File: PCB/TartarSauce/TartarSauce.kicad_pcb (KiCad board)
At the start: 2 copper layers, 118.1 x 76.2 mm, 46 parts, among them J1 Thumbstick, J2 OLED, J3 Conn_01x02, J4 Conn_01x02, U1 Teensy4.0, U2 MIC4801

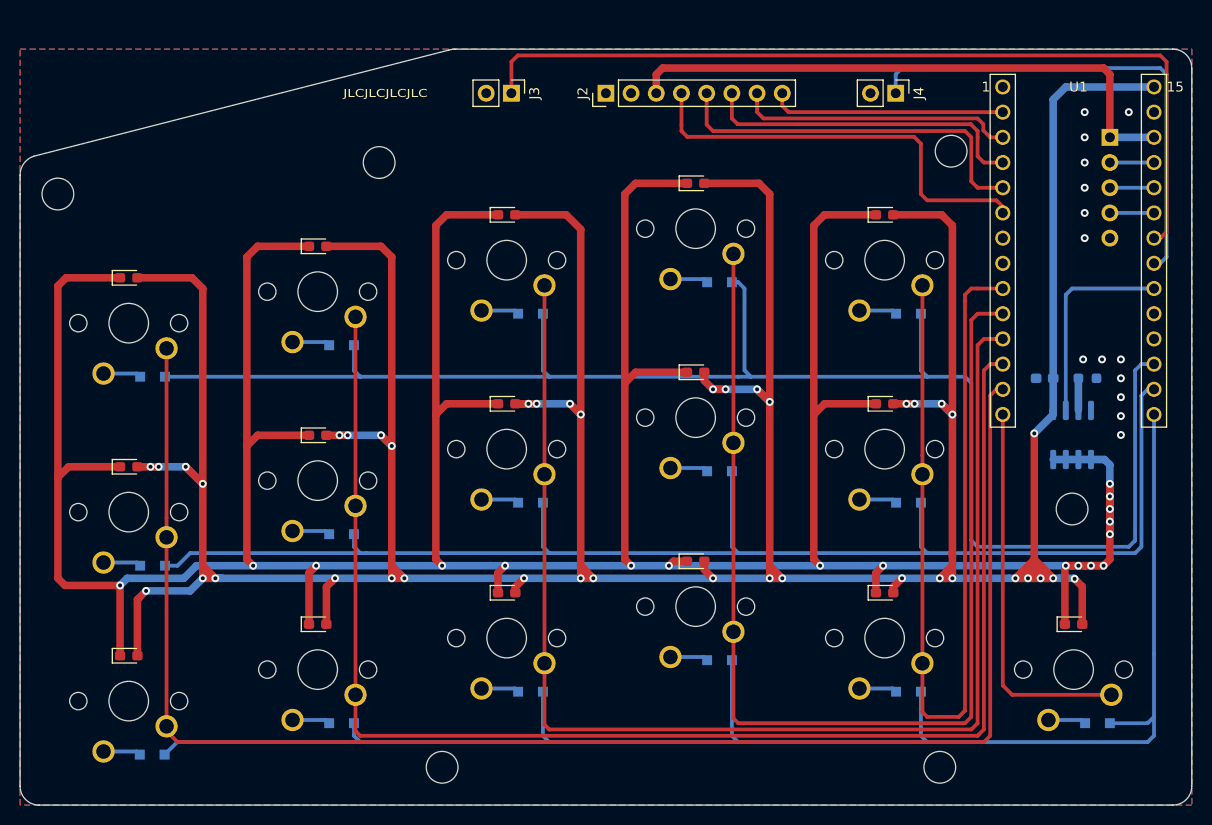
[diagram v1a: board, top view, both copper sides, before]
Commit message: Changed project to PlatformIO, added bitmaps and saved STL files to repo
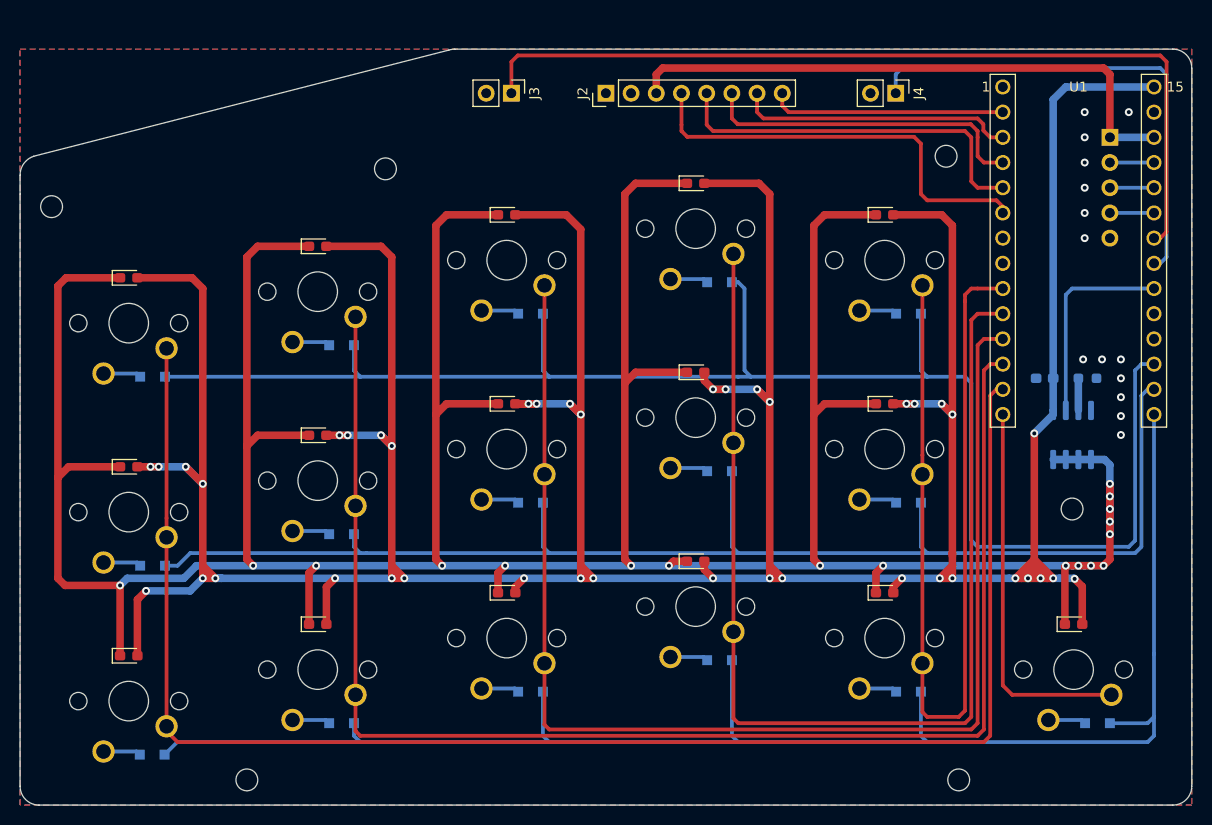
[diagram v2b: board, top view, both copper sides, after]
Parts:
- removed the REF** at (123.1, 42.7)
- removed the REF** at (135.3, 78.7)
- removed the REF** at (65.4, 43.8)
- removed the REF** at (33.0, 47.0)
- removed the REF** at (71.8, 104.8)
- removed the REF** at (121.9, 104.8)
- added REF**: MountingHole_2.2mm_M2, MountingHole:MountingHole_2.2mm_M2, F.Cu at (135.3, 78.7)
- added REF**: MountingHole_2.2mm_M2, MountingHole:MountingHole_2.2mm_M2, F.Cu at (123.8, 106.0)
- added REF**: MountingHole_2.2mm_M2, MountingHole:MountingHole_2.2mm_M2, F.Cu at (52.1, 106.0)
- added REF**: MountingHole_2.2mm_M2, MountingHole:MountingHole_2.2mm_M2, F.Cu at (66.0, 44.5)
- added REF**: MountingHole_2.2mm_M2, MountingHole:MountingHole_2.2mm_M2, F.Cu at (122.6, 43.2)
- added REF**: MountingHole_2.2mm_M2, MountingHole:MountingHole_2.2mm_M2, F.Cu at (32.4, 48.3)

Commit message: Joystick works now, but isn't scaled properly
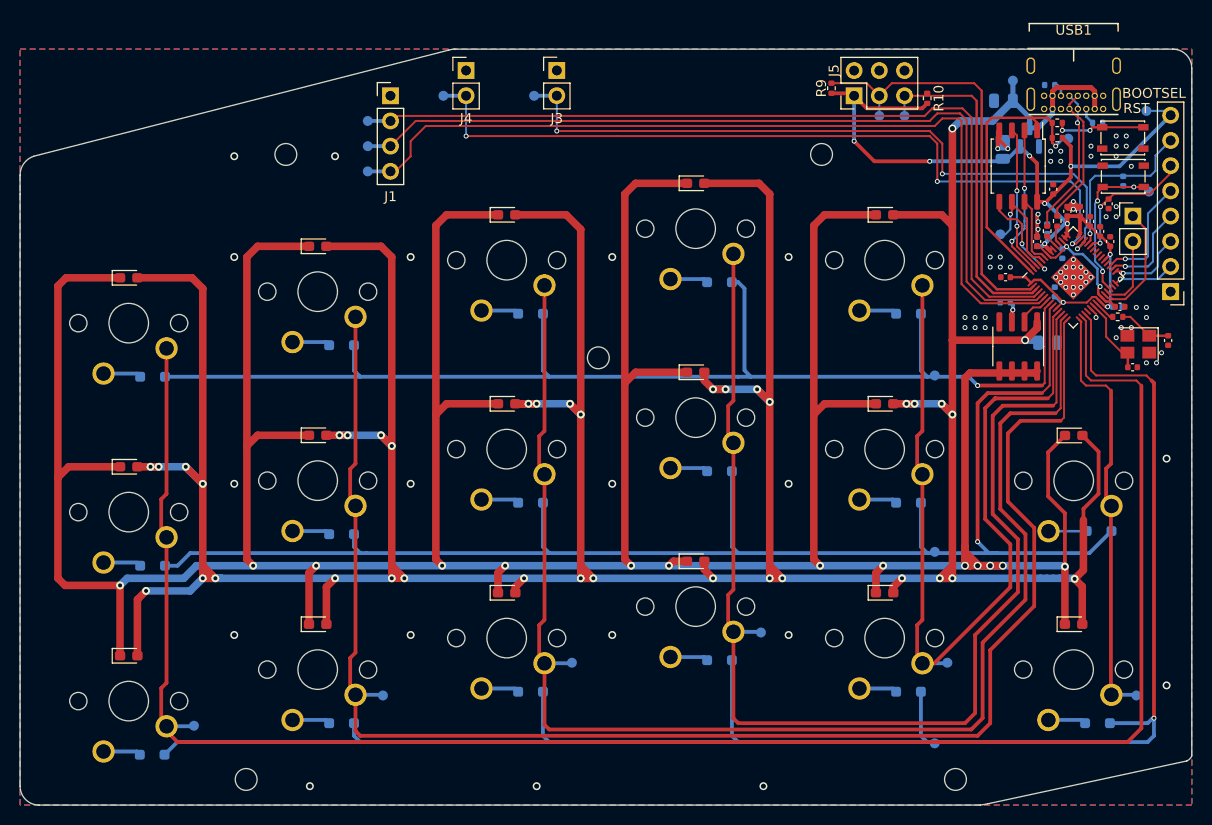
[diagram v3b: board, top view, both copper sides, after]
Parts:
- removed the REF** at (135.3, 78.7)
- removed the REF** at (123.8, 106.0)
- removed the REF** at (52.1, 106.0)
- removed the REF** at (66.0, 44.5)
- removed the REF** at (122.6, 43.2)
- removed the REF** at (32.4, 48.3)
- removed U1: Teensy4.0, _MCU_Devboards:Teensy4.0
- added C10: 0.1u, Capacitor_SMD:C_0402_1005Metric, F.Cu at (138.1, 50.8)
- added C11: 0.1u, Capacitor_SMD:C_0402_1005Metric, F.Cu at (137.1, 49.7)
- added C12: 0.1u, Capacitor_SMD:C_0402_1005Metric, F.Cu at (128.6, 55.4)
- added C13: 0.1u, Capacitor_SMD:C_0402_1005Metric, B.Cu at (133.5, 56.9)
- added C14: 0.1u, Capacitor_SMD:C_0402_1005Metric, B.Cu at (139.8, 58.4)
- added C15: 0.1u, Capacitor_SMD:C_0402_1005Metric, F.Cu at (133.3, 46.5)
- added C16: 27p, Capacitor_SMD:C_0402_1005Metric, F.Cu at (141.4, 64.5)
- added C17: 27p, Capacitor_SMD:C_0402_1005Metric, F.Cu at (144.9, 61.8)
- added C18: 10u, Capacitor_SMD:C_0805_2012Metric, B.Cu at (128.3, 37.6)
- added C19: 10u, Capacitor_SMD:C_0805_2012Metric, B.Cu at (128.3, 42.5)
- added C2: 1u, Capacitor_SMD:C_0402_1005Metric, B.Cu at (134.3, 53.0)
- added C20: 1n, Capacitor_SMD:C_0402_1005Metric, B.Cu at (140.4, 45.7)
- added C21: 1n, Capacitor_SMD:C_0402_1005Metric, F.Cu at (138.9, 48.0)
- added C3: 0.1u, Capacitor_SMD:C_0402_1005Metric, F.Cu at (131.7, 51.8)
- added C4: 0.1u, Capacitor_SMD:C_0402_1005Metric, F.Cu at (140.1, 58.4)
- added C5: 1u, Capacitor_SMD:C_0402_1005Metric, F.Cu at (136.0, 48.7)
- added C6: 0.1u, Capacitor_SMD:C_0402_1005Metric, B.Cu at (132.7, 50.5)
- added C7: 0.1u, Capacitor_SMD:C_0402_1005Metric, F.Cu at (134.8, 48.7)
- added C8: 0.1u, Capacitor_SMD:C_0402_1005Metric, F.Cu at (139.1, 51.8)
- added C9: 0.1u, Capacitor_SMD:C_0402_1005Metric, B.Cu at (131.7, 51.8)
- added D17: D, Diode_SMD:D_SOD-323_HandSoldering, B.Cu at (138.0, 81.0)
- added J5: OLED, Connector_PinHeader_2.54mm:PinHeader_2x03_P2.54mm_Vertical, F.Cu at (113.3, 37.1)
- added J6: DBG, Connector_PinHeader_2.54mm:PinHeader_1x02_P2.54mm_Vertical, F.Cu at (141.4, 49.2)
- added MX17: MX-LED, MX_Only:MXOnly-1U, F.Cu at (125.9, 66.4)
- added R10: 5k1, Resistor_SMD:R_0402_1005Metric, F.Cu at (120.7, 37.3)
- added R2: DNP, Resistor_SMD:R_0402_1005Metric, F.Cu at (133.8, 41.3)
- added R3: 1k, Resistor_SMD:R_0402_1005Metric, F.Cu at (133.8, 39.8)
- added R4: 1k, Resistor_SMD:R_0402_1005Metric, F.Cu at (139.9, 59.4)
- added R5: 5k1, Resistor_SMD:R_0402_1005Metric, B.Cu at (137.8, 39.8)
- added R6: 5k1, Resistor_SMD:R_0402_1005Metric, B.Cu at (133.0, 36.0)
- added R7: 27R, Resistor_SMD:R_0402_1005Metric, F.Cu at (133.8, 49.7)
- added R8: 27R, Resistor_SMD:R_0402_1005Metric, F.Cu at (132.7, 50.7)
- added R9: 5k1, Resistor_SMD:R_0402_1005Metric, F.Cu at (111.0, 36.3)
- added REF**: MountingHole_2.2mm_M2, MountingHole:MountingHole_2.2mm_M2, F.Cu at (110.0, 43.0)
- added REF**: MountingHole_2.2mm_M2, MountingHole:MountingHole_2.2mm_M2, F.Cu at (87.5, 63.5)
- added REF**: MountingHole_2.2mm_M2, MountingHole:MountingHole_2.2mm_M2, F.Cu at (52.0, 106.0)
- added REF**: MountingHole_2.2mm_M2, MountingHole:MountingHole_2.2mm_M2, F.Cu at (56.0, 43.0)
- added REF**: MountingHole_2.2mm_M2, MountingHole:MountingHole_2.2mm_M2, F.Cu at (123.5, 106.0)
- added SW1: BOOTSEL, Button_Switch_SMD:SW_SPST_PTS810, F.Cu at (140.4, 41.3)
- added SW2: RST, Button_Switch_SMD:SW_SPST_PTS810, F.Cu at (140.4, 45.2)
- added TP1: ROW0, TestPoint:TestPoint_Pad_D1.0mm, B.Cu at (121.4, 65.3)
- added TP10: SDA, TestPoint:TestPoint_Pad_D1.0mm, B.Cu at (115.8, 39.1)
- added TP11: SCL, TestPoint:TestPoint_Pad_D1.0mm, B.Cu at (118.4, 39.1)
- added TP13: ENCA, TestPoint:TestPoint_Pad_D1.0mm, B.Cu at (64.3, 39.6)
- added TP14: ENCB, TestPoint:TestPoint_Pad_D1.0mm, B.Cu at (64.3, 42.2)
- added TP15: ENCC, TestPoint:TestPoint_Pad_D1.0mm, B.Cu at (64.3, 44.7)
- added TP16: MISCA, TestPoint:TestPoint_Pad_D1.0mm, B.Cu at (81.0, 37.1)
- added TP17: MISCB, TestPoint:TestPoint_Pad_D1.0mm, B.Cu at (71.9, 37.1)
- added TP2: ROW1, TestPoint:TestPoint_Pad_D1.0mm, B.Cu at (121.4, 83.1)
- added TP28: SCK, TestPoint:TestPoint_Pad_D1.0mm, B.Cu at (128.0, 51.1)
- added TP29: SCK, TestPoint:TestPoint_Pad_D1.0mm, B.Cu at (134.9, 41.4)
- added TP3: ROW2, TestPoint:TestPoint_Pad_D1.0mm, B.Cu at (121.4, 102.4)
- added TP31: RUN, TestPoint:TestPoint_Pad_D1.0mm, B.Cu at (143.0, 46.7)
- added TP32: 5V, TestPoint:TestPoint_Pad_D1.0mm, B.Cu at (129.3, 35.6)
- added TP33: 3V3, TestPoint:TestPoint_Pad_D1.0mm, B.Cu at (142.7, 38.6)
- added TP4: COL0, TestPoint:TestPoint_Pad_D1.0mm, B.Cu at (46.7, 100.6)
- added TP5: COL1, TestPoint:TestPoint_Pad_D1.0mm, B.Cu at (65.8, 97.5)
- added TP6: COL2, TestPoint:TestPoint_Pad_D1.0mm, B.Cu at (84.8, 94.2)
- added TP7: COL3, TestPoint:TestPoint_Pad_D1.0mm, B.Cu at (103.9, 91.2)
- added TP8: COL4, TestPoint:TestPoint_Pad_D1.0mm, B.Cu at (122.7, 94.2)
- added TP9: COL5, TestPoint:TestPoint_Pad_D1.0mm, B.Cu at (141.7, 97.5)
- added U3: RP2040, Package_DFN_QFN:QFN-56-1EP_7x7mm_P0.4mm_EP3.2x3.2mm, F.Cu at (135.4, 55.4)
- added U4: W25Q128JVS, Package_SO:SOIC-8_5.23x5.23mm_P1.27mm, F.Cu at (129.8, 44.2)
- added U5: AP2127N-3.3, Package_TO_SOT_SMD:SOT-23, B.Cu at (131.0, 41.3)
- added USB1: USB4085-GF-A-Type-C, patchez_connectors:USB_C_GCT_USB4085, F.Cu at (135.4, 32.3)
- added Y1: 12MHz_18pf_30ppm, Crystal:Crystal_SMD_3225-4Pin_3.2x2.5mm, F.Cu at (141.9, 62.1)
- C1: value 2.2u -> 10u; footprint Capacitor_SMD:C_0603_1608Metric_Pad1.08x0.95mm_HandSolder -> Capacitor_SMD:C_0805_2012Metric
- J1: value Thumbstick -> Encoder; footprint Connector_PinHeader_2.54mm:PinHeader_1x05_P2.54mm_Vertical -> Connector_PinHeader_2.54mm:PinHeader_1x04_P2.54mm_Vertical; moved to F.Cu
- J2: value OLED -> Thumbstick
- J3, J4: value Conn_01x02 -> MISC_A
- MX1, MX10, MX11, MX12, MX13, MX14, MX15, MX18, MX2, MX3, MX4, MX5, MX6, MX7, MX8, MX9: footprint _MX_Only:MXOnly-1U -> MX_Only:MXOnly-1U
- R1: footprint Resistor_SMD:R_0603_1608Metric_Pad0.98x0.95mm_HandSolder -> Resistor_SMD:R_0402_1005Metric
- U2: moved to F.Cu
- moved J1 72.6 mm to (66.5, 37.1), turned to 0 degrees
- moved J2 60.3 mm to (145.2, 56.8), turned to 180 degrees
- moved J4 43.4 mm to (74.2, 34.5), turned to 0 degrees
- moved R1 11.3 mm to (128.5, 57.9), turned to 0 degrees
- moved U2 10.4 mm to (129.8, 62.4)
- moved J3 5.12 mm to (83.3, 34.5), turned to 0 degrees
- moved C1 3.60 mm to (132.8, 62.0), turned to 180 degrees
- renumbered D17 to D18
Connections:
- net /Col[0] renamed /Col0
- net /Col[1] renamed /Col1
- net /Col[2] renamed /Col2
- net /Col[3] renamed /Col3
- net /Col[4] renamed /Col4
- net /Row[0] renamed /Row0
- net /Row[1] renamed /Row1
- net /Row[2] renamed /Row2
- net LED_CAT renamed /LED_CAT
- J1 pad 1: +3V3 -> GND
- J1 pad 2: THUMB_VERT -> /ENCODER_A
- J1 pad 3: THUMB_HORI -> /ENCODER_B
- J1 pad 4: THUMB_L3 -> /ENCODER_C
- J2 pad 2: Net-(J2-Pad2) -> /THUMB_JMP
- J2 pad 3: +3V3 -> /THUMB_L3
- J2 pad 4: OLED_DATA -> /THUMB_DX-
- J2 pad 5: OLED_CLK -> /THUMB_DY-
- J2 pad 6: OLED_D_C -> /THUMB_AX_DX+
- J2 pad 7: OLED_RST -> /THUMB_AY_DY+
- J2 pad 8: OLED_CS -> +3V3
- J3 pad 1: MISC_0 -> GND
- J3 pad 2: GND -> /MISC_A
- J4 pad 1: MISC_1 -> GND
- J4 pad 2: GND -> /MISC_B
- MX18 pad 1: /Col[5] -> /Col5
- U2 pad 2: LED_EN -> /LED_EN
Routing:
- net MISC_0: track 89.1 -> 0.00 mm
- net /ENCODER_C: track 0.00 -> 89.0 mm
- net /ENCODER_B: track 0.00 -> 86.9 mm
- net /ENCODER_A: track 0.00 -> 85.8 mm
- net /MISC_B: track 0.00 -> 79.6 mm, vias 0 -> 3
- net /MISC_A: track 0.00 -> 71.1 mm, vias 0 -> 3
- net MISC_1: track 49.7 -> 0.00 mm
- net +3V3: track 58.9 -> 105.7 mm, vias 0 -> 10
- net /Col5: track 0.00 -> 43.4 mm
- net /OLED_I2C_SDA: track 0.00 -> 43.0 mm
- net OLED_DATA: track 43.0 -> 0.00 mm
- net /Col[5]: track 38.6 -> 0.00 mm
- net OLED_CLK: track 38.3 -> 0.00 mm
- net /Row0: track 161.1 -> 124.8 mm, vias 0 -> 1
- net /OLED_I2C_SCL: track 0.00 -> 34.1 mm
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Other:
- outline, holes or cut-outs redrawn
- net class Default removed
